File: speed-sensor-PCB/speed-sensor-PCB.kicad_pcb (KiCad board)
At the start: 2 copper layers, 62.2 x 62.2 mm, 8 parts, among them IC1 AS5600-ASOT, J1 Conn_01x03_Pin

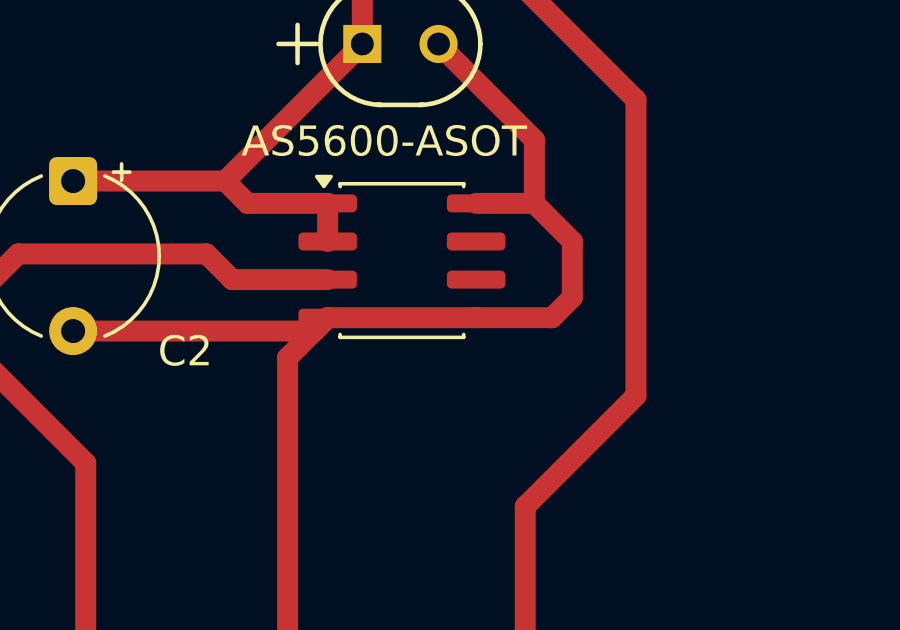
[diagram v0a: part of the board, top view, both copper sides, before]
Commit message: working on program, fixed PGO connection on speed detector PCB
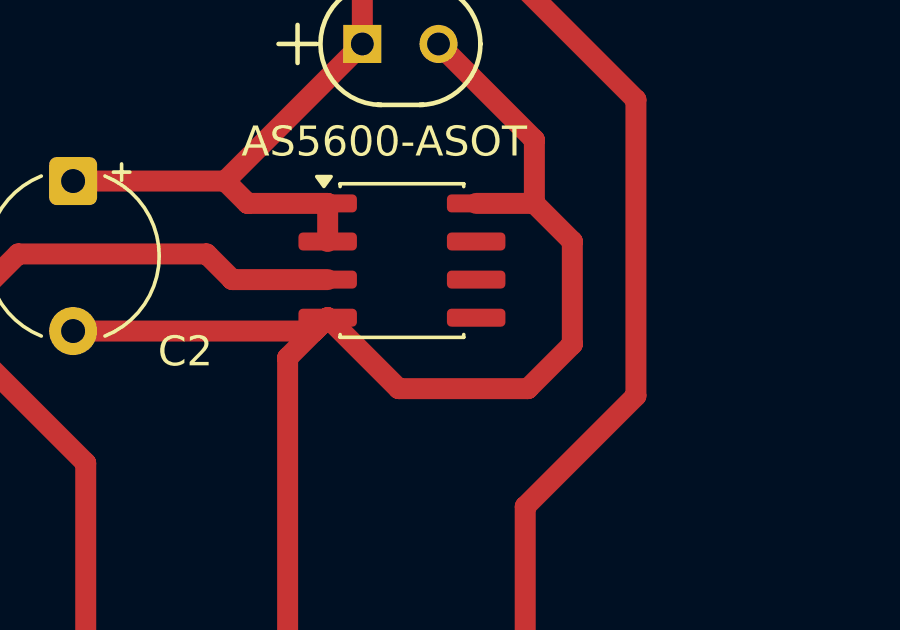
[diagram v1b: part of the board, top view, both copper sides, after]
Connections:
- IC1 pad 5: GND -> unconnected-(IC1-PGO-Pad5)
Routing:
- net GND: track 47.6 -> 50.4 mm
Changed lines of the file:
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@@
 	(net 4 "unconnected-(IC1-SCL-Pad7)")
 	(net 5 "Net-(IC1-OUT)")
+	(net 6 "unconnected-(IC1-PGO-Pad5)")
 	(footprint "MountingHole:MountingHole_3.2mm_M3_ISO7380"
 		(layer "F.Cu")
@@
 			(layers "F.Cu" "F.Mask" "F.Paste")
 			(roundrect_rratio 0.25)
-			(net 1 "GND")
+			(net 6 "unconnected-(IC1-PGO-Pad5)")
 			(pinfunction "PGO")
-			(pintype "passive")
+			(pintype "passive+no_connect")
 		)
 		(pad "6" smd roundrect
@@
 	)
 	(segment
-		(start 102.475 101.905)
-		(end 105.005 101.905)
+		(start 99.89 104.27)
+		(end 104.2 104.27)
 		(width 0.7)
 		(layer "F.Cu")
@@
 	)
 	(segment
-		(start 105.005 101.905)
-		(end 105.68 101.23)
-		(width 0.7)
-		(layer "F.Cu")
-		(net 1)
-	)
-	(segment
 		(start 97.08 102.35)
 		(end 97.525 101.905)
@@
 	)
 	(segment
-		(start 97.525 101.905)
-		(end 102.475 101.905)
+		(start 105.68 99.36)
+		(end 104.415 98.095)
 		(width 0.7)
 		(layer "F.Cu")
@@
 	)
 	(segment
+		(start 97.525 101.905)
+		(end 99.89 104.27)
+		(width 0.7)
+		(layer "F.Cu")
+		(net 1)
+	)
+	(segment
 		(start 104.415 98.095)
 		(end 102.475 98.095)
+		(width 0.7)
+		(layer "F.Cu")
+		(net 1)
+	)
+	(segment
+		(start 105.68 102.79)
+		(end 105.68 99.36)
 		(width 0.7)
 		(layer "F.Cu")
@@
 	)
 	(segment
-		(start 105.68 99.36)
-		(end 104.415 98.095)
+		(start 104.2 104.27)
+		(end 105.68 102.79)
 		(width 0.7)
 		(layer "F.Cu")
-		(net 1)
-	)
-	(segment
-		(start 105.68 101.23)
-		(end 105.68 99.36)
-		(width 0.7)
-		(layer "F.Cu")
